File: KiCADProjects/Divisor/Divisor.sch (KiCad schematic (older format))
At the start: 34 parts, among them J1 SMA_Female, J10 SMA_Female, J11 SMA_Female, J12 SMA_Female, J13 SMA_Female, J14 SMA_Female, J15 SMA_Female, J16 SMA_Female, J17 SMA_Female, J2 SMA_Female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

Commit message: Revisión 1.1 de PCBs
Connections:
- wire segments 21 -> 20
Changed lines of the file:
@@
 	6250 4150 6250 4900
 Connection ~ 7025 3150
-Wire Wire Line
-	7025 3150 7025 3650
-Connection ~ 7025 3650
-Wire Wire Line
-	7025 3650 7025 4150
 Connection ~ 7025 4150
 Wire Wire Line
@@
 	1    0    0    -1
 $EndComp
+Wire Wire Line
+	7025 3150 7025 4150
 $EndSCHEMATC

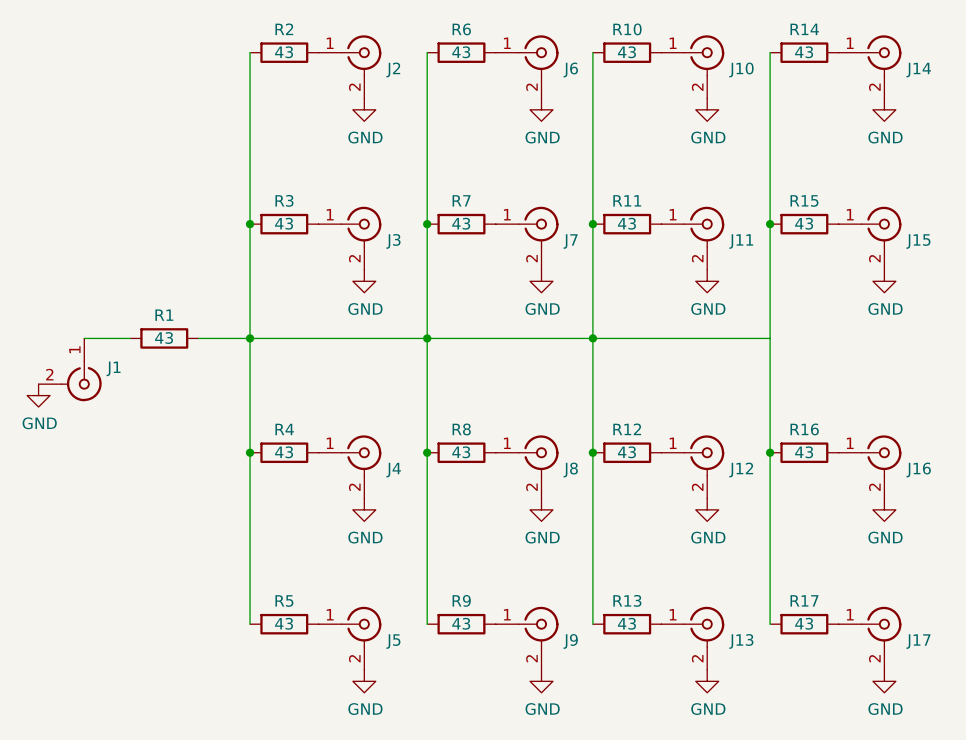
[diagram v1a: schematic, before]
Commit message: Modificaciones varias al divisor
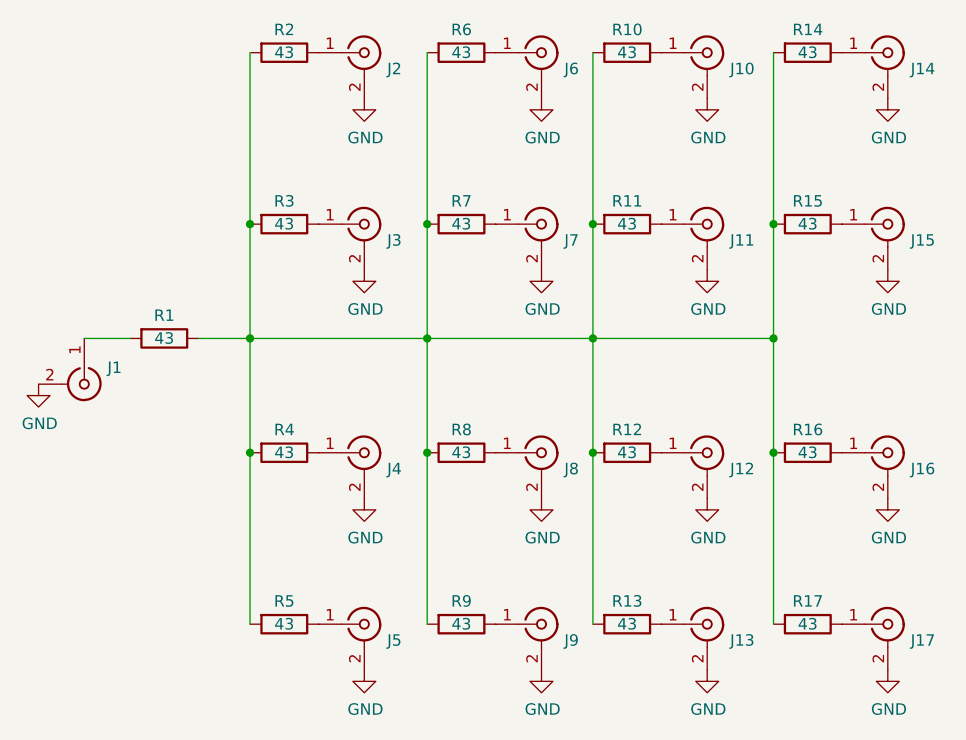
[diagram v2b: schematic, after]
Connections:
- wire segments 20 -> 22
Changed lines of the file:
@@
-$EndComp
-$Comp
-L Connector:Conn_Coaxial J16
-U 1 1 5EAA1929
-P 7525 4150
-F 0 "J16" H 7625 4079 50  0000 L CNN
-F 1 "SMA_Female" H 7625 4034 50  0001 L CNN
-F 2 "Connector_Coaxial:SMA_Samtec_SMA-J-P-X-ST-EM1_EdgeMount" H 7525 4150 50  0001 C CNN
-F 3 " ~" H 7525 4150 50  0001 C CNN
-	1    7525 4150
-	1    0    0    -1
-$EndComp
-$Comp
-L Connector:Conn_Coaxial J17
-U 1 1 5EAA192F
-P 7525 4900
-F 0 "J17" H 7625 4829 50  0000 L CNN
-F 1 "SMA_Female" H 7625 4784 50  0001 L CNN
-F 2 "Connector_Coaxial:SMA_Samtec_SMA-J-P-X-ST-EM1_EdgeMount" H 7525 4900 50  0001 C CNN
-F 3 " ~" H 7525 4900 50  0001 C CNN
-	1    7525 4900
-	1    0    0    -1
-$EndComp
-$Comp
-L Connector:Conn_Coaxial J15
-U 1 1 5EAA1935
-P 7525 3150
-F 0 "J15" H 7625 3079 50  0000 L CNN
-F 1 "SMA_Female" H 7625 3034 50  0001 L CNN
-F 2 "Connector_Coaxial:SMA_Samtec_SMA-J-P-X-ST-EM1_EdgeMount" H 7525 3150 50  0001 C CNN
-F 3 " ~" H 7525 3150 50  0001 C CNN
-	1    7525 3150
-	1    0    0    -1
-$EndComp
-$Comp
-L Connector:Conn_Coaxial J14
-U 1 1 5EAA193B
-P 7525 2400
-F 0 "J14" H 7625 2329 50  0000 L CNN
-F 1 "SMA_Female" H 7625 2284 50  0001 L CNN
-F 2 "Connector_Coaxial:SMA_Samtec_SMA-J-P-X-ST-EM1_EdgeMount" H 7525 2400 50  0001 C CNN
-F 3 " ~" H 7525 2400 50  0001 C CNN
-	1    7525 2400
-	1    0    0    -1
 $EndComp
 $Comp
@@
 $EndComp
 $Comp
-L power:GND #PWR014
-U 1 1 5EAA7B95
-P 7525 2600
-F 0 "#PWR014" H 7525 2350 50  0001 C CNN
-F 1 "GND" H 7530 2427 50  0000 C CNN
-F 2 "" H 7525 2600 50  0001 C CNN
-F 3 "" H 7525 2600 50  0001 C CNN
-	1    7525 2600
-	1    0    0    -1
-$EndComp
-$Comp
-L power:GND #PWR015
-U 1 1 5EAA82AD
-P 7525 3350
-F 0 "#PWR015" H 7525 3100 50  0001 C CNN
-F 1 "GND" H 7530 3177 50  0000 C CNN
-F 2 "" H 7525 3350 50  0001 C CNN
-F 3 "" H 7525 3350 50  0001 C CNN
-	1    7525 3350
-	1    0    0    -1
-$EndComp
-$Comp
 L power:GND #PWR011
 U 1 1 5EAA91D4
@@
 $EndComp
 $Comp
-L power:GND #PWR016
-U 1 1 5EAAB782
-P 7525 4350
-F 0 "#PWR016" H 7525 4100 50  0001 C CNN
-F 1 "GND" H 7530 4177 50  0000 C CNN
-F 2 "" H 7525 4350 50  0001 C CNN
-F 3 "" H 7525 4350 50  0001 C CNN
-	1    7525 4350
-	1    0    0    -1
-$EndComp
-$Comp
-L power:GND #PWR017
-U 1 1 5EAABE17
-P 7525 5100
-F 0 "#PWR017" H 7525 4850 50  0001 C CNN
-F 1 "GND" H 7530 4927 50  0000 C CNN
-F 2 "" H 7525 5100 50  0001 C CNN
-F 3 "" H 7525 5100 50  0001 C CNN
-	1    7525 5100
-	1    0    0    -1
-$EndComp
-$Comp
 L power:GND #PWR013
 U 1 1 5EAAC522
@@
 Wire Wire Line
 	6250 2400 6250 3150
-Wire Wire Line
-	7025 2400 7025 3150
 $Comp
 L Device:R R10
@@
 	0    1    1    0
 $EndComp
-$Comp
-L Device:R R14
-U 1 1 5EAF4B97
-P 7175 2400
-F 0 "R14" V 7075 2400 50  0000 C CNN
-F 1 "43" V 7175 2400 50  0000 C CNN
-F 2 "Resistor_SMD:R_0805_2012Metric_Pad1.15x1.40mm_HandSolder" V 7105 2400 50  0001 C CNN
-F 3 "~" H 7175 2400 50  0001 C CNN
-	1    7175 2400
-	0    1    1    0
-$EndComp
-$Comp
-L Device:R R15
-U 1 1 5EAF4B9D
-P 7175 3150
-F 0 "R15" V 7075 3150 50  0000 C CNN
-F 1 "43" V 7175 3150 50  0000 C CNN
-F 2 "Resistor_SMD:R_0805_2012Metric_Pad1.15x1.40mm_HandSolder" V 7105 3150 50  0001 C CNN
-F 3 "~" H 7175 3150 50  0001 C CNN
-	1    7175 3150
-	0    1    1    0
-$EndComp
-$Comp
-L Device:R R16
-U 1 1 5EAF4BA3
-P 7175 4150
-F 0 "R16" V 7075 4150 50  0000 C CNN
-F 1 "43" V 7175 4150 50  0000 C CNN
-F 2 "Resistor_SMD:R_0805_2012Metric_Pad1.15x1.40mm_HandSolder" V 7105 4150 50  0001 C CNN
-F 3 "~" H 7175 4150 50  0001 C CNN
-	1    7175 4150
-	0    1    1    0
-$EndComp
-$Comp
-L Device:R R17
-U 1 1 5EAF4BA9
-P 7175 4900
-F 0 "R17" V 7075 4900 50  0000 C CNN
-F 1 "43" V 7175 4900 50  0000 C CNN
-F 2 "Resistor_SMD:R_0805_2012Metric_Pad1.15x1.40mm_HandSolder" V 7105 4900 50  0001 C CNN
-F 3 "~" H 7175 4900 50  0001 C CNN
-	1    7175 4900
-	0    1    1    0
-$EndComp
 Wire Wire Line
 	4025 3650 4225 3650
@@
 Wire Wire Line
 	6250 4150 6250 4900
-Connection ~ 7025 3150
-Connection ~ 7025 4150
-Wire Wire Line
-	7025 4150 7025 4900
 Wire Wire Line
 	5525 3650 6250 3650
@@
 Connection ~ 6250 3150
 Connection ~ 6250 3650
-Wire Wire Line
-	6250 3650 7025 3650
 Wire Wire Line
 	6250 3650 6250 4150
@@
 $EndComp
 Wire Wire Line
-	7025 3150 7025 4150
+	6245 3650 6250 3650
+Wire Wire Line
+	7040 3150 7040 3650
+Connection ~ 7040 4150
+Connection ~ 7040 3150
+Wire Wire Line
+	7040 4150 7040 4900
+$Comp
+L Device:R R17
+U 1 1 5F435B6B
+P 7190 4900
+F 0 "R17" V 7090 4900 50  0000 C CNN
+F 1 "43" V 7190 4900 50  0000 C CNN
+F 2 "Resistor_SMD:R_0805_2012Metric_Pad1.15x1.40mm_HandSolder" V 7120 4900 50  0001 C CNN
+F 3 "~" H 7190 4900 50  0001 C CNN
+	1    7190 4900
+	0    1    1    0
+$EndComp
+$Comp
+L Device:R R16
+U 1 1 5F435B65
+P 7190 4150
+F 0 "R16" V 7090 4150 50  0000 C CNN
+F 1 "43" V 7190 4150 50  0000 C CNN
+F 2 "Resistor_SMD:R_0805_2012Metric_Pad1.15x1.40mm_HandSolder" V 7120 4150 50  0001 C CNN
+F 3 "~" H 7190 4150 50  0001 C CNN
+	1    7190 4150
+	0    1    1    0
+$EndComp
+$Comp
+L Device:R R15
+U 1 1 5F435B5F
+P 7190 3150
+F 0 "R15" V 7090 3150 50  0000 C CNN
+F 1 "43" V 7190 3150 50  0000 C CNN
+F 2 "Resistor_SMD:R_0805_2012Metric_Pad1.15x1.40mm_HandSolder" V 7120 3150 50  0001 C CNN
+F 3 "~" H 7190 3150 50  0001 C CNN
+	1    7190 3150
+	0    1    1    0
+$EndComp
+$Comp
+L Device:R R14
+U 1 1 5F435B59
+P 7190 2400
+F 0 "R14" V 7090 2400 50  0000 C CNN
+F 1 "43" V 7190 2400 50  0000 C CNN
+F 2 "Resistor_SMD:R_0805_2012Metric_Pad1.15x1.40mm_HandSolder" V 7120 2400 50  0001 C CNN
+F 3 "~" H 7190 2400 50  0001 C CNN
+	1    7190 2400
+	0    1    1    0
+$EndComp
+Wire Wire Line
+	7040 2400 7040 3150
+$Comp
+L power:GND #PWR017
+U 1 1 5F435B52
+P 7540 5100
+F 0 "#PWR017" H 7540 4850 50  0001 C CNN
+F 1 "GND" H 7545 4927 50  0000 C CNN
+F 2 "" H 7540 5100 50  0001 C CNN
+F 3 "" H 7540 5100 50  0001 C CNN
+	1    7540 5100
+	1    0    0    -1
+$EndComp
+$Comp
+L power:GND #PWR016
+U 1 1 5F435B4C
+P 7540 4350
+F 0 "#PWR016" H 7540 4100 50  0001 C CNN
+F 1 "GND" H 7545 4177 50  0000 C CNN
+F 2 "" H 7540 4350 50  0001 C CNN
+F 3 "" H 7540 4350 50  0001 C CNN
+	1    7540 4350
+	1    0    0    -1
+$EndComp
+$Comp
+L power:GND #PWR015
+U 1 1 5F435B46
+P 7540 3350
+F 0 "#PWR015" H 7540 3100 50  0001 C CNN
+F 1 "GND" H 7545 3177 50  0000 C CNN
+F 2 "" H 7540 3350 50  0001 C CNN
+F 3 "" H 7540 3350 50  0001 C CNN
+	1    7540 3350
+	1    0    0    -1
+$EndComp
+$Comp
+L power:GND #PWR014
+U 1 1 5F435B40
+P 7540 2600
+F 0 "#PWR014" H 7540 2350 50  0001 C CNN
+F 1 "GND" H 7545 2427 50  0000 C CNN
+F 2 "" H 7540 2600 50  0001 C CNN
+F 3 "" H 7540 2600 50  0001 C CNN
+	1    7540 2600
+	1    0    0    -1
+$EndComp
+$Comp
+L Connector:Conn_Coaxial J14
+U 1 1 5F435B3A
+P 7540 2400
+F 0 "J14" H 7640 2329 50  0000 L CNN
+F 1 "SMA_Female" H 7640 2284 50  0001 L CNN
+F 2 "Connector_Coaxial:SMA_Samtec_SMA-J-P-X-ST-EM1_EdgeMount" H 7540 2400 50  0001 C CNN
+F 3 " ~" H 7540 2400 50  0001 C CNN
+	1    7540 2400
+	1    0    0    -1
+$EndComp
+$Comp
+L Connector:Conn_Coaxial J15
+U 1 1 5F435B34
+P 7540 3150
+F 0 "J15" H 7640 3079 50  0000 L CNN
+F 1 "SMA_Female" H 7640 3034 50  0001 L CNN
+F 2 "Connector_Coaxial:SMA_Samtec_SMA-J-P-X-ST-EM1_EdgeMount" H 7540 3150 50  0001 C CNN
+F 3 " ~" H 7540 3150 50  0001 C CNN
+	1    7540 3150
+	1    0    0    -1
+$EndComp
+$Comp
+L Connector:Conn_Coaxial J17
+U 1 1 5F435B2E
+P 7540 4900
+F 0 "J17" H 7640 4829 50  0000 L CNN
+F 1 "SMA_Female" H 7640 4784 50  0001 L CNN
+F 2 "Connector_Coaxial:SMA_Samtec_SMA-J-P-X-ST-EM1_EdgeMount" H 7540 4900 50  0001 C CNN
+F 3 " ~" H 7540 4900 50  0001 C CNN
+	1    7540 4900
+	1    0    0    -1
+$EndComp
+$Comp
+L Connector:Conn_Coaxial J16
+U 1 1 5F435B28
+P 7540 4150
+F 0 "J16" H 7640 4079 50  0000 L CNN
+F 1 "SMA_Female" H 7640 4034 50  0001 L CNN
+F 2 "Connector_Coaxial:SMA_Samtec_SMA-J-P-X-ST-EM1_EdgeMount" H 7540 4150 50  0001 C CNN
+F 3 " ~" H 7540 4150 50  0001 C CNN
+	1    7540 4150
+	1    0    0    -1
+$EndComp
+Wire Wire Line
+	6250 3650 7040 3650
+Connection ~ 7040 3650
+Wire Wire Line
+	7040 3650 7040 4150
 $EndSCHEMATC

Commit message: Versión con sys clk a 100 MHz. Archivos de proyecto
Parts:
- R1, R10, R11, R12, R13, R14, R15, R16, R17, R2, R3, R6, R7, R8, R9: value 43 -> 44.1
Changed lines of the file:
@@
 P 4375 3650
 F 0 "R1" V 4275 3650 50  0000 C CNN
-F 1 "43" V 4375 3650 50  0000 C CNN
+F 1 "44.1" V 4375 3650 50  0000 C CNN
 F 2 "Resistor_SMD:R_0805_2012Metric_Pad1.15x1.40mm_HandSolder" V 4305 3650 50  0001 C CNN
 F 3 "~" H 4375 3650 50  0001 C CNN
@@
 P 4900 2400
 F 0 "R2" V 4800 2400 50  0000 C CNN
-F 1 "43" V 4900 2400 50  0000 C CNN
+F 1 "44.1" V 4900 2400 50  0000 C CNN
 F 2 "Resistor_SMD:R_0805_2012Metric_Pad1.15x1.40mm_HandSolder" V 4830 2400 50  0001 C CNN
 F 3 "~" H 4900 2400 50  0001 C CNN
@@
 P 4900 3150
 F 0 "R3" V 4800 3150 50  0000 C CNN
-F 1 "43" V 4900 3150 50  0000 C CNN
+F 1 "44.1" V 4900 3150 50  0000 C CNN
 F 2 "Resistor_SMD:R_0805_2012Metric_Pad1.15x1.40mm_HandSolder" V 4830 3150 50  0001 C CNN
 F 3 "~" H 4900 3150 50  0001 C CNN
@@
 P 5675 2400
 F 0 "R6" V 5575 2400 50  0000 C CNN
-F 1 "43" V 5675 2400 50  0000 C CNN
+F 1 "44.1" V 5675 2400 50  0000 C CNN
 F 2 "Resistor_SMD:R_0805_2012Metric_Pad1.15x1.40mm_HandSolder" V 5605 2400 50  0001 C CNN
 F 3 "~" H 5675 2400 50  0001 C CNN
@@
 P 5675 3150
 F 0 "R7" V 5575 3150 50  0000 C CNN
-F 1 "43" V 5675 3150 50  0000 C CNN
+F 1 "44.1" V 5675 3150 50  0000 C CNN
 F 2 "Resistor_SMD:R_0805_2012Metric_Pad1.15x1.40mm_HandSolder" V 5605 3150 50  0001 C CNN
 F 3 "~" H 5675 3150 50  0001 C CNN
@@
 P 5675 4150
 F 0 "R8" V 5575 4150 50  0000 C CNN
-F 1 "43" V 5675 4150 50  0000 C CNN
+F 1 "44.1" V 5675 4150 50  0000 C CNN
 F 2 "Resistor_SMD:R_0805_2012Metric_Pad1.15x1.40mm_HandSolder" V 5605 4150 50  0001 C CNN
 F 3 "~" H 5675 4150 50  0001 C CNN
@@
 P 5675 4900
 F 0 "R9" V 5575 4900 50  0000 C CNN
-F 1 "43" V 5675 4900 50  0000 C CNN
+F 1 "44.1" V 5675 4900 50  0000 C CNN
 F 2 "Resistor_SMD:R_0805_2012Metric_Pad1.15x1.40mm_HandSolder" V 5605 4900 50  0001 C CNN
 F 3 "~" H 5675 4900 50  0001 C CNN
@@
 P 6400 2400
 F 0 "R10" V 6300 2400 50  0000 C CNN
-F 1 "43" V 6400 2400 50  0000 C CNN
+F 1 "44.1" V 6400 2400 50  0000 C CNN
 F 2 "Resistor_SMD:R_0805_2012Metric_Pad1.15x1.40mm_HandSolder" V 6330 2400 50  0001 C CNN
 F 3 "~" H 6400 2400 50  0001 C CNN
@@
 P 6400 3150
 F 0 "R11" V 6300 3150 50  0000 C CNN
-F 1 "43" V 6400 3150 50  0000 C CNN
+F 1 "44.1" V 6400 3150 50  0000 C CNN
 F 2 "Resistor_SMD:R_0805_2012Metric_Pad1.15x1.40mm_HandSolder" V 6330 3150 50  0001 C CNN
 F 3 "~" H 6400 3150 50  0001 C CNN
@@
 P 6400 4150
 F 0 "R12" V 6300 4150 50  0000 C CNN
-F 1 "43" V 6400 4150 50  0000 C CNN
+F 1 "44.1" V 6400 4150 50  0000 C CNN
 F 2 "Resistor_SMD:R_0805_2012Metric_Pad1.15x1.40mm_HandSolder" V 6330 4150 50  0001 C CNN
 F 3 "~" H 6400 4150 50  0001 C CNN
@@
 P 6400 4900
 F 0 "R13" V 6300 4900 50  0000 C CNN
-F 1 "43" V 6400 4900 50  0000 C CNN
+F 1 "44.1" V 6400 4900 50  0000 C CNN
 F 2 "Resistor_SMD:R_0805_2012Metric_Pad1.15x1.40mm_HandSolder" V 6330 4900 50  0001 C CNN
 F 3 "~" H 6400 4900 50  0001 C CNN
@@
 P 7190 4900
 F 0 "R17" V 7090 4900 50  0000 C CNN
-F 1 "43" V 7190 4900 50  0000 C CNN
+F 1 "44.1" V 7190 4900 50  0000 C CNN
 F 2 "Resistor_SMD:R_0805_2012Metric_Pad1.15x1.40mm_HandSolder" V 7120 4900 50  0001 C CNN
 F 3 "~" H 7190 4900 50  0001 C CNN
@@
 P 7190 4150
 F 0 "R16" V 7090 4150 50  0000 C CNN
-F 1 "43" V 7190 4150 50  0000 C CNN
+F 1 "44.1" V 7190 4150 50  0000 C CNN
 F 2 "Resistor_SMD:R_0805_2012Metric_Pad1.15x1.40mm_HandSolder" V 7120 4150 50  0001 C CNN
 F 3 "~" H 7190 4150 50  0001 C CNN
@@
 P 7190 3150
 F 0 "R15" V 7090 3150 50  0000 C CNN
-F 1 "43" V 7190 3150 50  0000 C CNN
+F 1 "44.1" V 7190 3150 50  0000 C CNN
 F 2 "Resistor_SMD:R_0805_2012Metric_Pad1.15x1.40mm_HandSolder" V 7120 3150 50  0001 C CNN
 F 3 "~" H 7190 3150 50  0001 C CNN
@@
 P 7190 2400
 F 0 "R14" V 7090 2400 50  0000 C CNN
-F 1 "43" V 7190 2400 50  0000 C CNN
+F 1 "44.1" V 7190 2400 50  0000 C CNN
 F 2 "Resistor_SMD:R_0805_2012Metric_Pad1.15x1.40mm_HandSolder" V 7120 2400 50  0001 C CNN
 F 3 "~" H 7190 2400 50  0001 C CNN
